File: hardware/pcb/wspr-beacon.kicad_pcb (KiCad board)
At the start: 2 copper layers, 100 x 70 mm, 76 parts, among them J1 USB_OTG, J2 Conn_01x04, J3 Conn_02x03_Odd_Even, J4 Conn_Coaxial, J5 Conn_Coaxial, J6 Conn_Coaxial, SW1 SW_Push, U1 AP1117-33, U2 ATMEGA328-AU, U3 Si5351A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

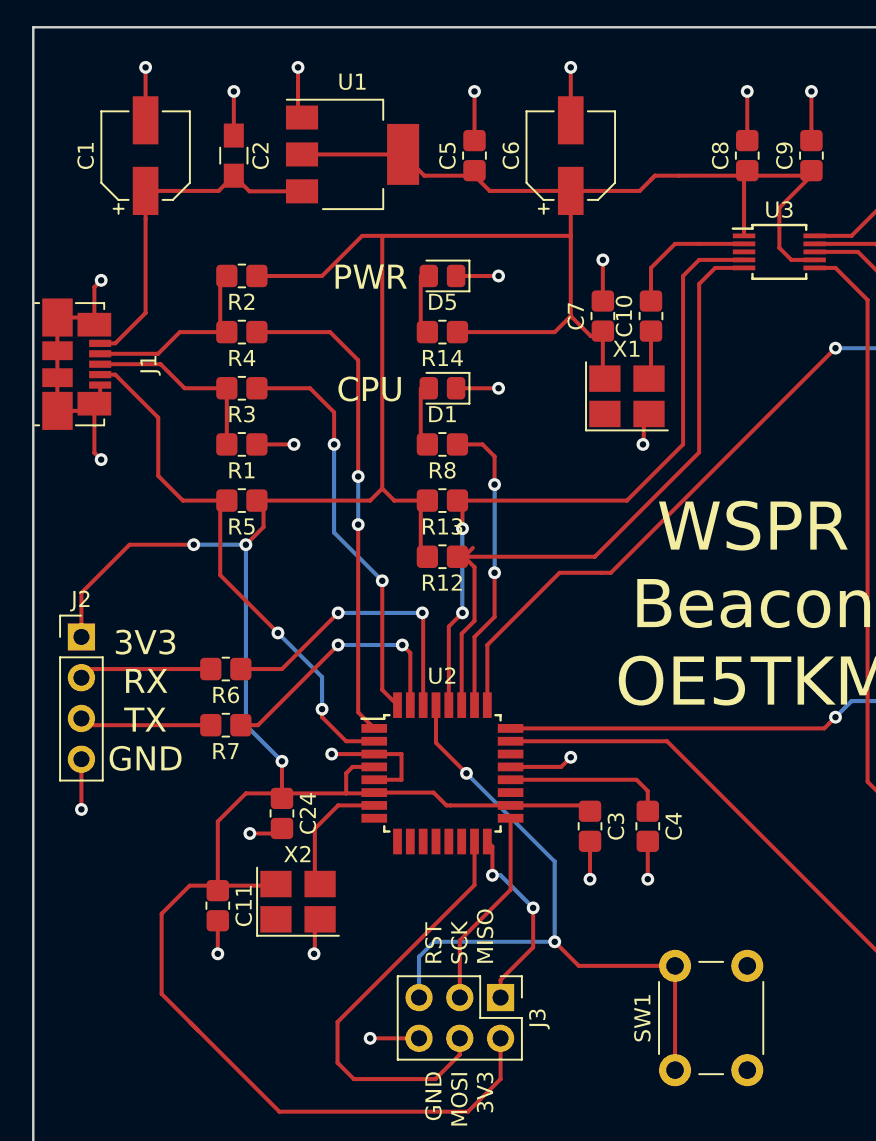
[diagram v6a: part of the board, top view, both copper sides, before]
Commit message: Minor layout and footprint changes
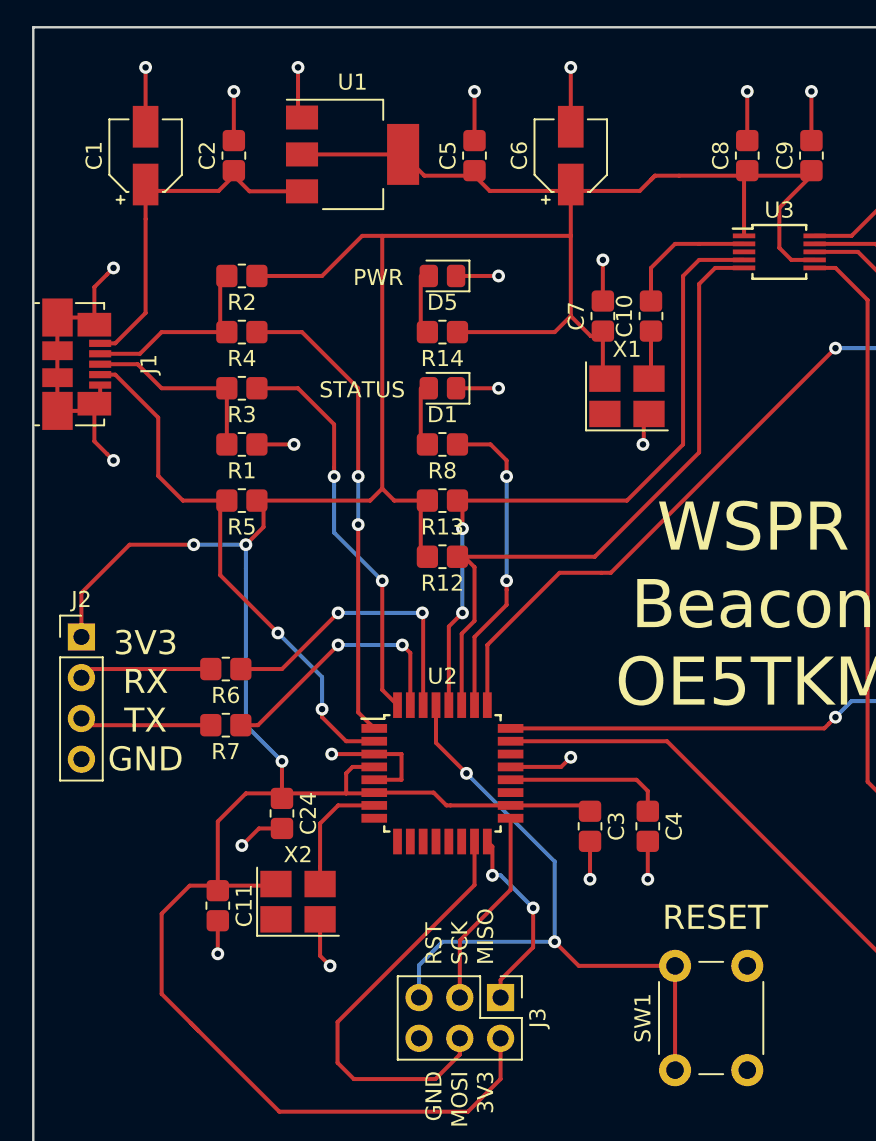
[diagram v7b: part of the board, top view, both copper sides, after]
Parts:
- C1, C6: footprint Capacitor_SMD:CP_Elec_5x5.4 -> Capacitor_SMD:CP_Elec_4x4.5
- C2: footprint Capacitors_SMD:C_0805_HandSoldering -> Capacitor_SMD:C_0805_2012Metric_Pad1.33x1.40mm_HandSolder
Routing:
- net GND: track 182.9 -> 179.8 mm, vias 45 -> 43
- net /LED_ACTIVE: track 18.2 -> 19.6 mm
- net /D-: track 30.3 -> 29.3 mm
- net /SDA: track 41.9 -> 41.1 mm
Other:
- board text added: "RESET"
- board text added: "STATUS"
- board text removed: "CPU"

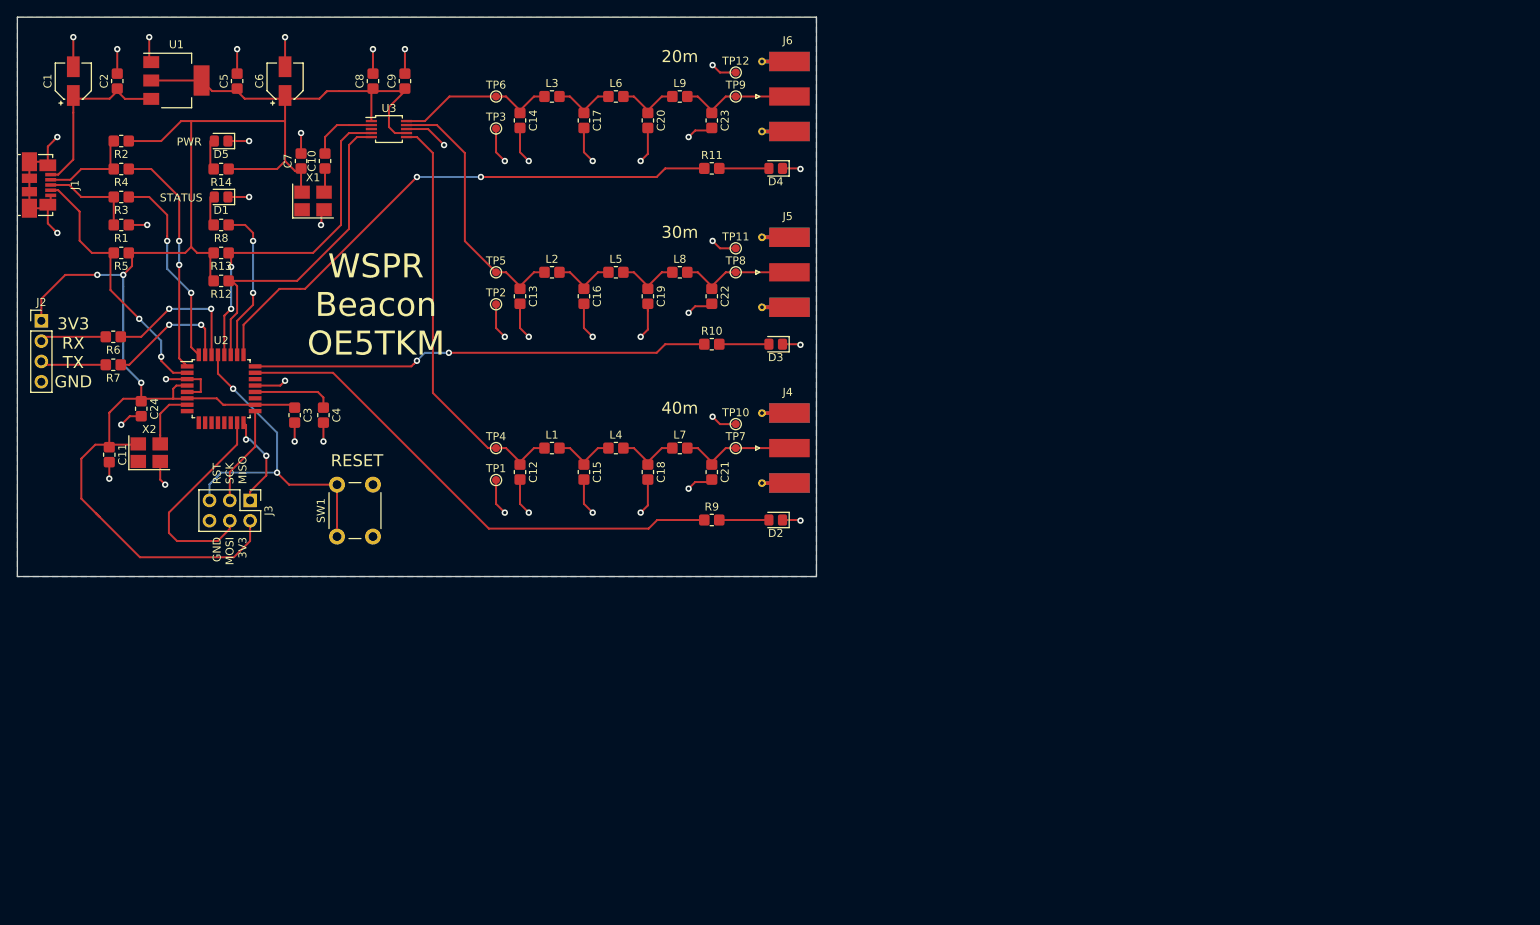
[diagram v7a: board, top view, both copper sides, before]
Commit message: Add attenuator to clock input of Si5351
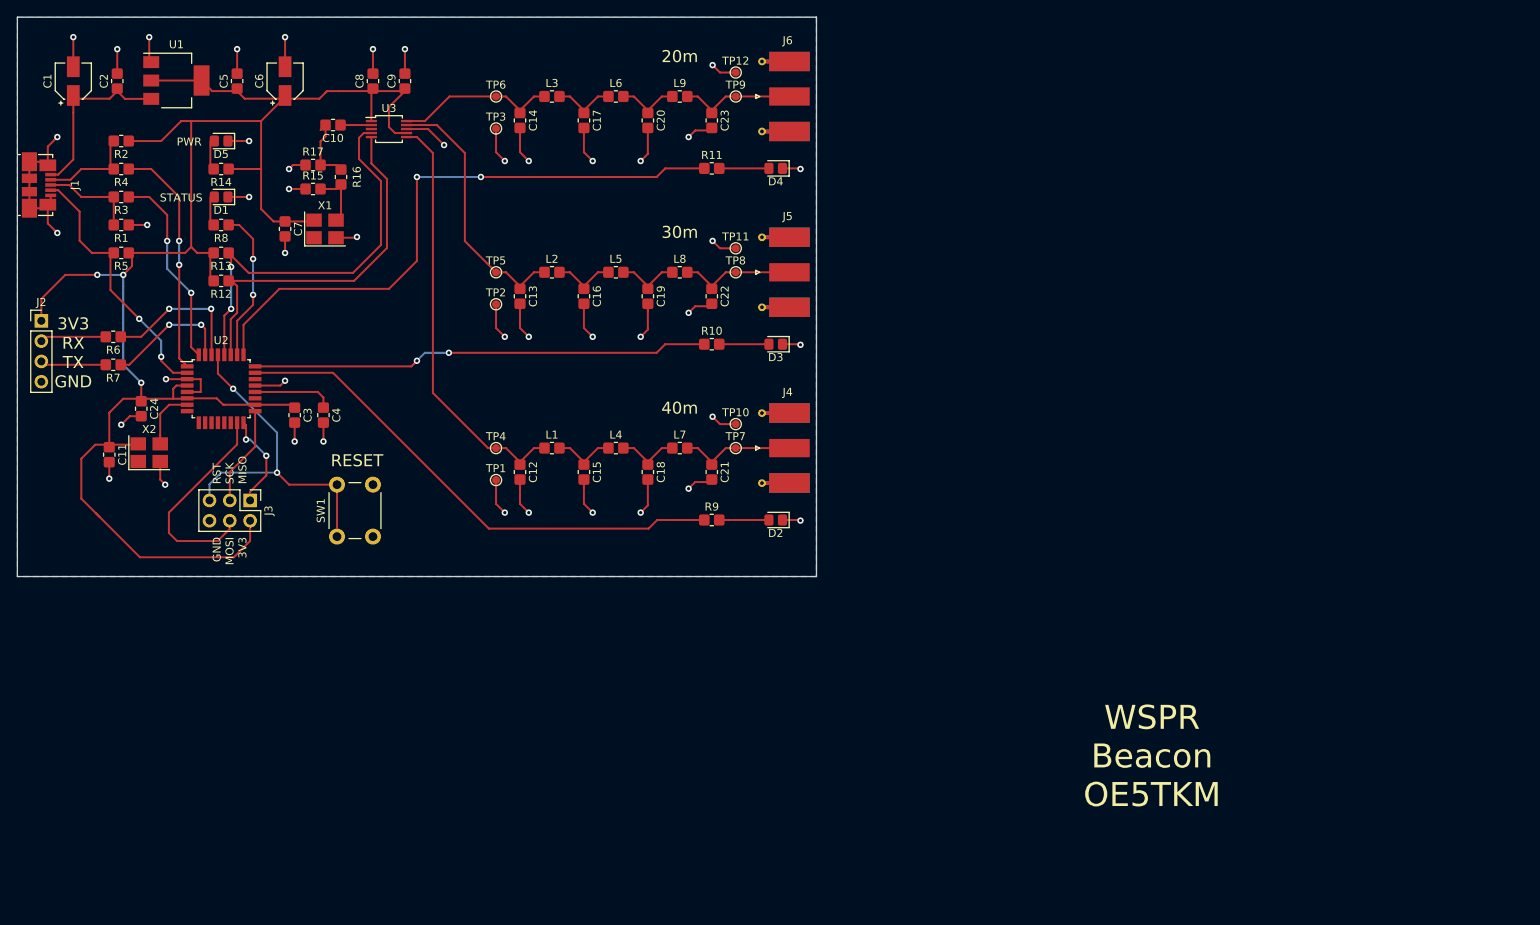
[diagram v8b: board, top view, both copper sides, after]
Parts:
- added R15: R, Resistor_SMD:R_0805_2012Metric_Pad1.33x1.40mm_HandSolder, F.Cu at (87.1, 71.6)
- added R16: R, Resistor_SMD:R_0805_2012Metric_Pad1.33x1.40mm_HandSolder, F.Cu at (90.6, 70.1)
- added R17: R, Resistor_SMD:R_0805_2012Metric_Pad1.33x1.40mm_HandSolder, F.Cu at (87.1, 68.6)
- moved C7 8.73 mm to (83.6, 76.6), turned to 270 degrees
- moved C10 4.61 mm to (89.6, 63.6), turned to 180 degrees
- moved X1 3.81 mm to (88.6, 76.6)
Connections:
- U3 pad 2: Net-(C10-Pad2) -> Net-(C10-Pad1)
- X1 pad 3: Net-(C10-Pad1) -> Net-(R15-Pad2)
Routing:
- net /SCL: track 43.3 -> 51.0 mm
- net Net-(R15-Pad2): track 0.00 -> 7.52 mm
- net /LED_40M: track 69.1 -> 75.3 mm
- net /SDA: track 41.1 -> 46.3 mm
- net GND: track 179.8 -> 184.2 mm, vias 43 -> 45
- net +3V3: track 223.7 -> 225.9 mm
- net Net-(C10-Pad1): track 3.11 -> 3.86 mm
- net Net-(C10-Pad2): track 8.42 -> 8.94 mm
